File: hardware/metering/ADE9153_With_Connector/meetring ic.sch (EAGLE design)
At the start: 38 parts, among them J9 AK300/2-5,0-GRAU, Y1 12.288mhz

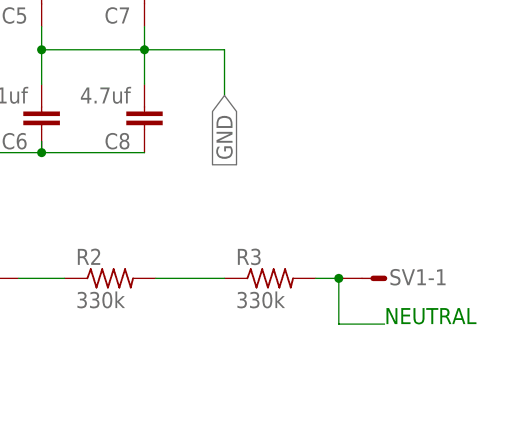
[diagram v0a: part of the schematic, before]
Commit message: change in metering IC design
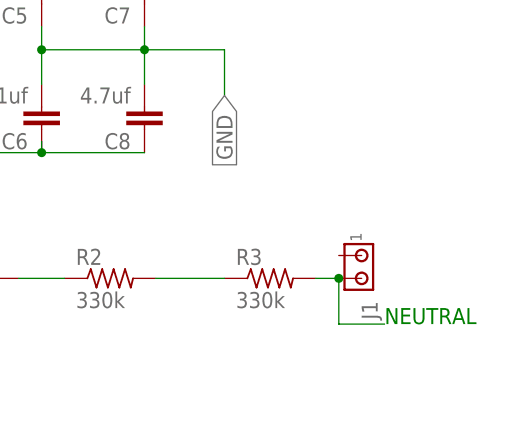
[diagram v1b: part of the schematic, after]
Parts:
- removed SV1: (no value), con-amp-mt6:MT6-3
- added J1: (no value), con-amp:MTA02-156
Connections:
- net N$27: now also J1.2; no longer SV1-1.S
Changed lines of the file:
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@@
 <part name="R10" library="rcl" library_urn="urn:adsk.eagle:library:334" deviceset="R-US_" device="0204/7" package3d_urn="urn:adsk.eagle:package:23498/2" value="10kohm"/>
 <part name="C23" library="capacitor-wima" library_urn="urn:adsk.eagle:library:116" deviceset="C" device="2.5/2" package3d_urn="urn:adsk.eagle:package:5415/1" value="0.1uf"/>
-<part name="SV1" library="con-amp-mt6" library_urn="urn:adsk.eagle:library:124" deviceset="MT6-3" device="" package3d_urn="urn:adsk.eagle:package:5885/1"/>
+<part name="J1" library="con-amp" library_urn="urn:adsk.eagle:library:127" deviceset="MTA02-156" device="" package3d_urn="urn:adsk.eagle:package:8081562/1"/>
 </parts>
 <sheets>
@@
 <attribute name="VALUE" x="112.014" y="85.471" size="1.778" layer="96"/>
 </instance>
-<instance part="SV1" gate="-1" x="147.32" y="-12.7" smashed="yes" rot="R180">
-<attribute name="NAME" x="147.828" y="-13.462" size="1.778" layer="95"/>
-<attribute name="VALUE" x="147.066" y="-10.287" size="1.778" layer="96" rot="R180"/>
+<instance part="J1" gate="G$1" x="144.78" y="-10.16" smashed="yes" rot="R270">
+<attribute name="NAME" x="144.78" y="-15.24" size="1.778" layer="95" rot="R270"/>
+<attribute name="VALUE" x="140.97" y="-15.24" size="1.778" layer="96" rot="R270"/>
 </instance>
 </instances>
@@
 <net name="N$27" class="0">
 <segment>
-<pinref part="SV1" gate="-1" pin="S"/>
 <pinref part="R3" gate="G$1" pin="2"/>
 <wire x1="142.24" y1="-12.7" x2="139.7" y2="-12.7" width="0.1524" layer="91"/>
 <wire x1="142.24" y1="-12.7" x2="142.24" y2="-17.78" width="0.1524" layer="91"/>
+<wire x1="142.24" y1="-17.78" x2="147.32" y2="-17.78" width="0.1524" layer="91"/>
+<pinref part="J1" gate="G$1" pin="2"/>
 <junction x="142.24" y="-12.7"/>
-<wire x1="142.24" y1="-17.78" x2="147.32" y2="-17.78" width="0.1524" layer="91"/>
-</segment>
-</net>
+</segment>
+</net>

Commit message: ADE9153Base
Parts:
- added U$2: LIB1OPTION_HOLE, esp32_base_footprint:LIB1OPTION_HOLE
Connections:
- net N$27: now also J1.1
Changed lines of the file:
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@@
 <setting verticaltext="up"/>
 </settings>
-<grid distance="0.1" unitdist="inch" unit="inch" style="lines" multiple="1" display="yes" altdistance="0.01" altunitdist="inch" altunit="mm"/>
+<grid distance="0.000000123031" unitdist="inch" unit="inch" style="lines" multiple="1" display="no" altdistance="0.003125" altunitdist="mic" altunit="mm"/>
 <layers>
 <layer number="1" name="Top" color="4" fill="1" visible="no" active="no"/>
@@
 <part name="C23" library="capacitor-wima" library_urn="urn:adsk.eagle:library:116" deviceset="C" device="2.5/2" package3d_urn="urn:adsk.eagle:package:5415/1" value="0.1uf"/>
 <part name="J1" library="con-amp" library_urn="urn:adsk.eagle:library:127" deviceset="MTA02-156" device="" package3d_urn="urn:adsk.eagle:package:8081562/1"/>
+<part name="U$2" library="esp32_base_footprint" deviceset="LIB1" device="OPTION_HOLE"/>
 </parts>
 <sheets>
@@
 <attribute name="VALUE" x="140.97" y="-15.24" size="1.778" layer="96" rot="R270"/>
 </instance>
+<instance part="U$2" gate="G$1" x="194.70918125" y="62.500184375" smashed="yes"/>
 </instances>
 <busses>
@@
 <segment>
 <pinref part="U$1" gate="G$1" pin="IBMS-19"/>
-<label x="104.14" y="35.56" size="1.778" layer="95" xref="yes"/>
+<label x="104.06916875" y="34.284584375" size="1.778" layer="95" xref="yes"/>
 <wire x1="93.98" y1="34.29" x2="101.6" y2="34.29" width="0.1524" layer="91"/>
-<wire x1="101.6" y1="34.29" x2="104.14" y2="35.56" width="0.1524" layer="91"/>
+<wire x1="101.6" y1="34.29" x2="104.06916875" y2="34.284584375" width="0.1524" layer="91"/>
 </segment>
 <segment>
@@
 <pinref part="U$1" gate="G$1" pin="DGND-20"/>
 <wire x1="93.98" y1="39.37" x2="96.52" y2="39.37" width="0.1524" layer="91"/>
-<wire x1="96.52" y1="39.37" x2="96.52" y2="40.64" width="0.1524" layer="91"/>
-<label x="96.52" y="40.64" size="1.778" layer="95" xref="yes"/>
+<wire x1="96.52" y1="39.37" x2="100.356890625" y2="39.370746875" width="0.1524" layer="91"/>
+<label x="100.356890625" y="39.370746875" size="1.778" layer="95" xref="yes"/>
 </segment>
 </net>
@@
 <pinref part="J1" gate="G$1" pin="2"/>
 <junction x="142.24" y="-12.7"/>
-</segment>
-</net>
+<pinref part="J1" gate="G$1" pin="1"/>
+<wire x1="142.24" y1="-10.16" x2="142.24" y2="-12.7" width="0.1524" layer="91"/>
+</segment>
+</net>
